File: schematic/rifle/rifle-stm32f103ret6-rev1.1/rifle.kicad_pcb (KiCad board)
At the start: 2 copper layers, 83.2 x 62.1 mm, 51 parts, among them K1 Magazine, K2 Sound, K3 IR_LASER, P1 Indication, P10 RFID-RC522-MODULE, P11 NRF24L01, P12 CONN_2, P13 IR_LED, P14 Power_in, P15 Power_out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

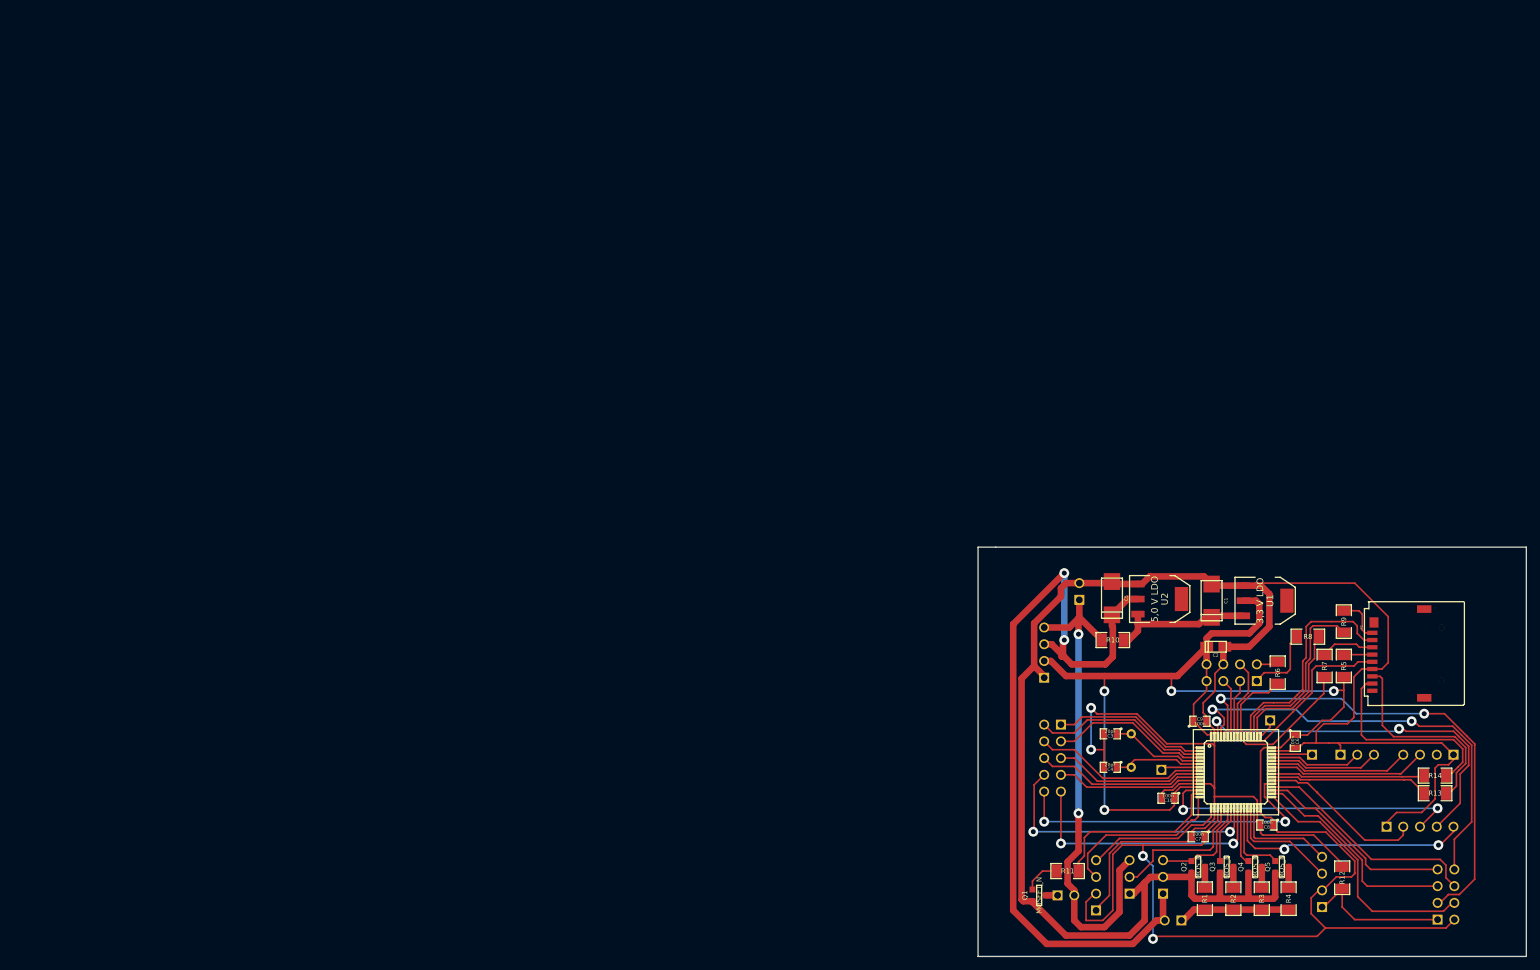
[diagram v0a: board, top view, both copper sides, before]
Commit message: Rifle r1.1 pcb beginned
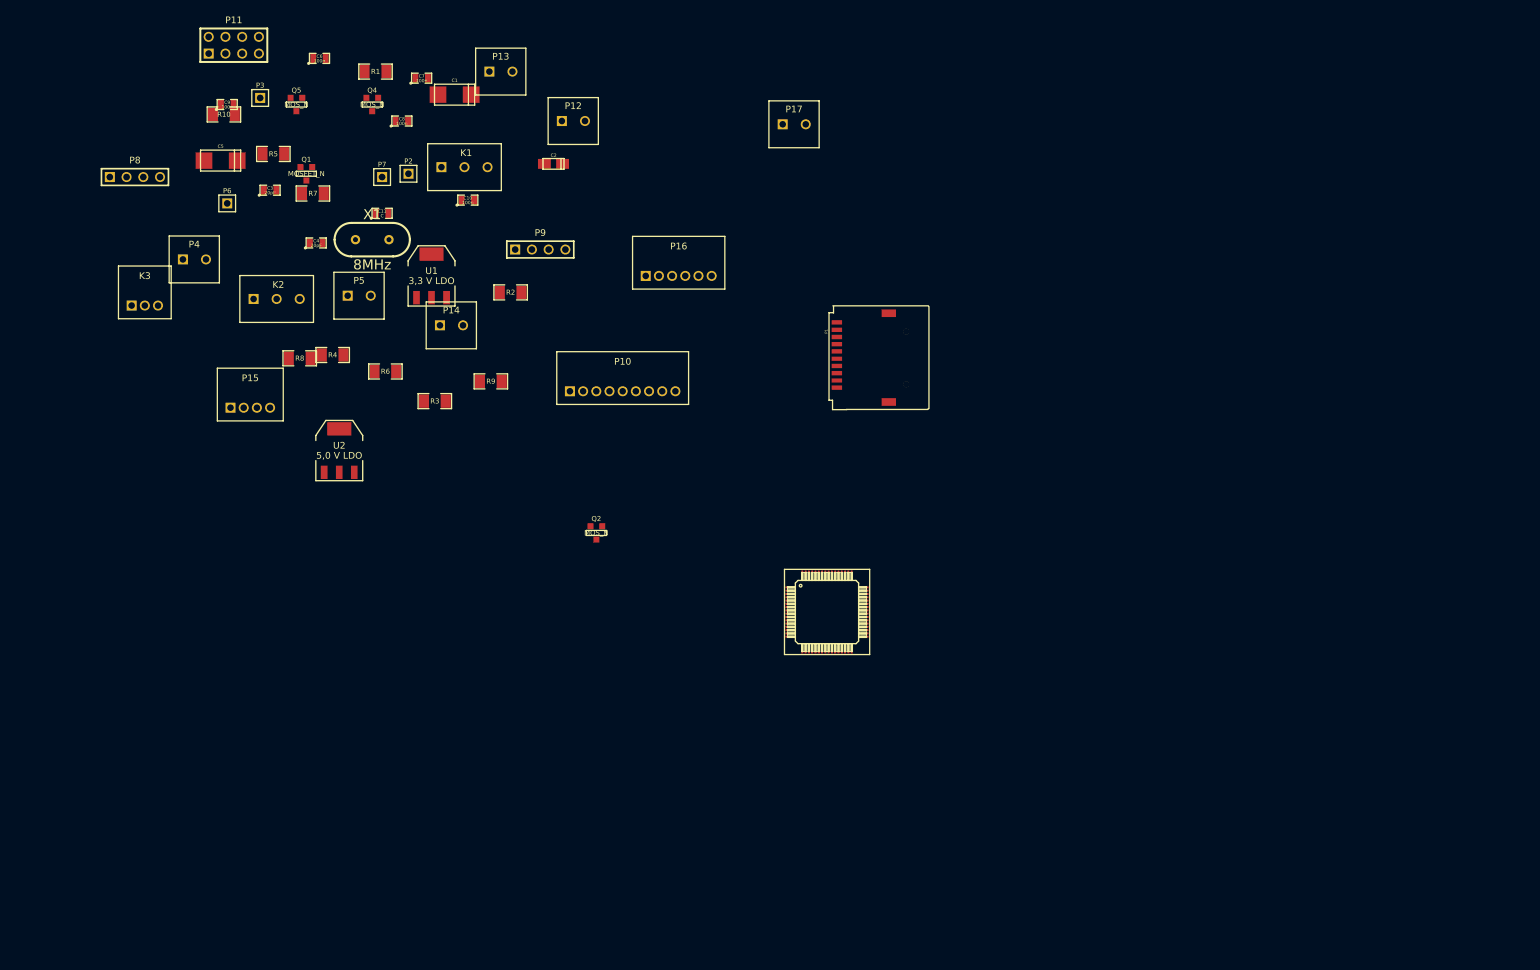
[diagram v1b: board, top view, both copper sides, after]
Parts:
- removed Q3: MOS_N, SOT23GDS
- removed R11, R12, R13, R14: 0, SM1206
- added C11: C, SM0805, F.Cu at (23.5, 22.5)
- added P16: Indicators, PIN_ARRAY-6X1-2mm-horiz, F.Cu at (68.5, 32.0)
- added P17: FireFlash, TERMINALS_2, F.Cu at (86.0, 9.00)
- K1: footprint PIN_ARRAY_3X1 -> TERMINALS_3; moved to F.Cu
- K2: value Sound -> Fire_mode; footprint PIN_ARRAY_3X1 -> TERMINALS_3; moved to F.Cu
- K3: footprint PIN_ARRAY_3X1 -> PIN_ARRAY-3X1-2mm-horiz; moved to F.Cu
- P1: value Indication -> MICROSD-SDIO-CD; footprint PIN_ARRAY_5x2 -> MICROSD-CD; moved to F.Cu
- P10: footprint pin_array_4x2 -> PIN_ARRAY-9X1-2mm-horiz; moved to F.Cu
- P11, P3, P6, P7, P8, P9, X1: moved to F.Cu
- P12: value CONN_2 -> VibroEng; footprint PIN_ARRAY_2X1 -> TERMINALS_2; moved to F.Cu
- P13, P14: footprint PIN_ARRAY_2X1 -> TERMINALS_2; moved to F.Cu
- P15: value Power_out -> Sound; footprint PIN_ARRAY_4x1 -> PIN_ARRAY-4X1-2mm-horiz; moved to F.Cu
- P2: value MICROSD-SDIO -> GND; footprint MICROSD -> PIN_ARRAY_1
- P4: value CONN_5 -> Reload; footprint PIN_ARRAY_5x1 -> TERMINALS_2; moved to F.Cu
- P5: value CONN_4 -> Fire; footprint PIN_ARRAY_4x1 -> TERMINALS_2; moved to F.Cu
- R1, R2: value R -> 47k
- R10, R8, R9: value 0 -> R
- R5, R6, R7: value 0 -> 47k
- moved P11 224.6 mm to (1.00, -3.00), turned to 0 degrees
- moved P4 204.9 mm to (-5.00, 29.5)
- moved Q5 189.0 mm to (10.5, 6.00), turned to 0 degrees
- moved P6 184.6 mm to (0.00, 21.0)
- moved P8 181.1 mm to (-14.0, 17.0), turned to 0 degrees
- moved C6 180.7 mm to (14.0, -1.00), turned to 0 degrees
- moved R5 180.0 mm to (7.00, 13.5), turned to 0 degrees
- moved R1 177.7 mm to (22.5, 1.00), turned to 0 degrees
- moved K3 177.1 mm to (-12.5, 36.5), turned to 0 degrees
- moved Q4 177.0 mm to (22.0, 6.00), turned to 0 degrees
- moved C9 174.7 mm to (0.00, 6.00)
- moved P5 171.1 mm to (20.0, 35.0), turned to 0 degrees
- moved P3 170.5 mm to (5.00, 5.00)
- moved R7 169.4 mm to (13.0, 19.5), turned to 0 degrees
- moved C8 169.2 mm to (26.5, 8.50), turned to 0 degrees
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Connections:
- C1 pad 1: N-0000049 -> +BATT
- K2 pad 2: N-0000063 -> N-0000032
- K2 pad 3: +BATT -> N-0000048
- K3 pad 3: N-0000058 -> N-000004
- P1 pad 1: N-0000057 -> N-0000035
- P1 pad 2: N-0000060 -> N-0000034
- P1 pad 3: N-0000061 -> N-0000033
- P1 pad 4: N-0000051 -> +3.3V
- P1 pad 5: N-0000052 -> N-0000016
- P1 pad 6: N-0000053 -> GND
- P1 pad 7: N-0000050 -> N-0000043
- P1 pad 8: N-0000069 -> N-0000053
- P10 pad 1: N-000009 (its old number) -> N-0000024
- P10 pad 2: N-0000033 -> N-0000051
- P11 pad 1: N-0000041 -> GND
- P13 pad 1: N-0000015 (its old number) -> N-0000030
- P15 pad 2: +3.3V -> N-0000040
- P15 pad 3: +5V -> N-0000044
- P2 pad 1: N-0000045 (its old number) -> GND
- P4 pad 2: N-0000035 -> N-0000050
- P5 pad 1: N-0000041 -> GND
- P5 pad 2: +3.3V -> N-0000031
- Q1 pad G: N-0000040 -> N-0000013
- Q2 pad D: N-0000016 -> N-0000038
- Q2 pad G: N-0000058 -> N-0000039
- Q4 pad G: N-0000013 -> N-000004
- R1 pad 1: N-0000015 (its old number) -> +3.3V
- R1 pad 2: N-0000016 -> N-0000053
- R10 pad 1: +BATT -> N-0000042
- R10 pad 2: N-0000049 -> N-0000040
- R2 pad 1: N-0000015 (its old number) -> +3.3V
- R2 pad 2: N-0000017 (its old number) -> N-0000043
- R3 pad 1: N-0000015 (its old number) -> N-0000030
- R4 pad 1: N-0000015 (its old number) -> N-0000030
- R5 pad 1: N-0000044 -> +3.3V
- R5 pad 2: +3.3V -> N-0000033
- R6 pad 1: N-0000034 -> +3.3V
- R6 pad 2: N-0000033 -> N-0000034
- R7 pad 1: N-0000047 (its old number) -> +3.3V
- R7 pad 2: N-0000056 -> N-0000035
- R8 pad 1: N-0000048 -> +BATT
- R8 pad 2: N-000009 (its old number) -> N-0000052
- R9 pad 1: N-0000045 (its old number) -> N-0000052
- R9 pad 2: N-0000046 -> GND
- U1 pad 3: N-0000049 -> +BATT
- U2 pad 3: N-0000049 -> +BATT
- U3 pad 10: N-0000053 -> (no net)
- U3 pad 11: N-0000050 -> (no net)
- U3 pad 14: N-0000038 -> N-0000031
- U3 pad 15: N-0000064 -> N-0000013
- U3 pad 2: N-0000057 -> (no net)
- U3 pad 20: N-0000063 -> N-0000042
- U3 pad 21: (no net) -> N-0000049
- U3 pad 22: N-0000058 -> N-0000046
- U3 pad 24: N-0000069 -> N-0000044
- U3 pad 25: N-0000070 -> (no net)
- U3 pad 26: N-0000013 -> N-000004
- U3 pad 28: N-0000032 -> N-0000050
- U3 pad 29: N-0000010 (its old number) -> (no net)
- U3 pad 3: N-0000060 -> (no net)
- U3 pad 30: N-0000011 (its old number) -> N-0000039
- U3 pad 37: N-0000062 -> N-0000032
- U3 pad 38: N-0000035 -> N-0000036
- U3 pad 39: N-0000068 -> N-0000043
- U3 pad 4: N-0000061 -> (no net)
- U3 pad 40: N-0000059 -> N-0000053
- U3 pad 41: (no net) -> N-0000054
- U3 pad 50: N-0000048 -> N-0000024
- U3 pad 51: N-0000046 -> N-0000035
- U3 pad 52: N-0000054 -> N-0000034
- U3 pad 53: N-0000055 -> N-0000016
- U3 pad 54: N-0000056 -> N-0000033
- U3 pad 55: N-0000034 -> N-0000051
- U3 pad 62: N-0000039 -> N-0000048
- U3 pad 8: N-0000051 -> N-0000052
- U3 pad 9: N-0000052 -> (no net)
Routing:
- net GND: track 391.3 -> 0.00 mm, vias 2 -> 0
- net +3.3V: track 288.3 -> 0.00 mm, vias 6 -> 0
- net +5V: track 121.9 -> 0.00 mm, vias 2 -> 0
- net +BATT: track 77.2 -> 0.00 mm, vias 2 -> 0
- net N-000001: track 74.9 -> 0.00 mm, vias 2 -> 0
- net N-0000011: track 66.6 -> 0.00 mm, vias 2 -> 0
- net N-0000039: track 56.5 -> 0.00 mm, vias 2 -> 0
- net N-0000062: track 49.5 -> 0.00 mm, vias 2 -> 0
- net N-0000038: track 48.3 -> 0.00 mm, vias 2 -> 0
- net N-0000069: track 42.7 -> 0.00 mm, vias 2 -> 0
- net N-0000070: track 39.4 -> 0.00 mm, vias 2 -> 0
- net N-0000010: track 38.4 -> 0.00 mm
- net N-0000032: track 38.4 -> 0.00 mm, vias 2 -> 0
- net N-000008: track 34.8 -> 0.00 mm
- net N-0000054: track 34.4 -> 0.00 mm
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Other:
- board outline removed
- net class Batt+ removed
- net class Default: clearance 0.2 -> 0.254; trace_width 1 -> 0.254; via_dia 1.5 -> 0.889; via_drill 1 -> 0.635
- rule trace_clearance: 0.2 -> 0.254

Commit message: WIP rifle 1.1 pcb
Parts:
- K1, K2, K3, P10, P11, P12, P13, P14, P15, P16, P17, P2, P3, P4, P5, P6, P7, P8, P9, X1: moved to B.Cu
- moved P11 140.3 mm to (108.8, 86.8), turned to 90 degrees
- moved P4 124.0 mm to (99.2, 96.7)
- moved K3 118.5 mm to (91.0, 94.3)
- moved P6 115.6 mm to (99.8, 79.4)
- moved P15 114.6 mm to (104.8, 105.5)
- moved P14 110.1 mm to (135.6, 81.8)
- moved P8 110.0 mm to (64.5, 94.1), turned to 270 degrees
- moved P3 107.4 mm to (77.8, 83.9)
- moved C8 107.2 mm to (97.0, 89.2)
- moved C6 104.4 mm to (85.0, 75.5), turned to 90 degrees
- moved C7 97.8 mm to (82.2, 84.4), turned to 90 degrees
- moved K1 94.3 mm to (107.1, 77.4)
- moved P7 93.2 mm to (96.5, 75.0)
- moved C3 92.5 mm to (79.0, 76.5), turned to 180 degrees
- moved P17 90.4 mm to (107.9, 96.7)
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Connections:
- P17 pad 2: (no net) -> +3.3V
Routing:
- net +3.3V: track 0.00 -> 15.5 mm
- net N-0000013: track 0.00 -> 11.8 mm
- net GND: track 0.00 -> 9.65 mm, vias 0 -> 5
- net N-0000023: track 0.00 -> 3.45 mm
- added copper zone on F.Cu, net +3.3V
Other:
- net class Default: clearance 0.254 -> 0.18; trace_width 0.254 -> 0.3; via_dia 0.889 -> 0.7; via_drill 0.635 -> 0.3
- rule trace_clearance: 0.254 -> 0.18
- rule trace_min: 0.254 -> 0.15
- rule via_min_drill: 0.508 -> 0.3
- rule via_min_size: 0.889 -> 0.7

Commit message: Rifle pcb seems done
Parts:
- P8: footprint PIN_ARRAY_4x1 -> PIN_ARRAY-4X1-2mm-horiz
- moved Q5 124.1 mm to (93.9, 97.9)
- moved C9 115.9 mm to (97.5, 68.6), turned to 270 degrees
- moved Q4 111.1 mm to (84.4, 97.9)
- moved R10 103.1 mm to (66.5, 85.8), turned to 90 degrees
- moved C5 102.5 mm to (84.3, 71.4), turned to 180 degrees
- moved R5 101.9 mm to (95.8, 63.5), turned to 90 degrees
- moved Q1 100.3 mm to (82.3, 88.0)
- moved R1 97.5 mm to (92.3, 69.0), turned to 270 degrees
- moved R4 91.0 mm to (89.2, 98.1)
- moved R7 89.1 mm to (90.5, 63.5), turned to 90 degrees
- moved R6 71.2 mm to (93.1, 63.5), turned to 90 degrees
- moved P14 67.8 mm to (72.8, 56.2)
- moved R3 67.0 mm to (79.6, 97.7)
- moved U1 62.6 mm to (84.2, 64.9), turned to 180 degrees
- moved P2 61.4 mm to (99.1, 55.9)
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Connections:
- P17 pad 2: +3.3V -> +BATT
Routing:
- net +BATT: track 0.00 -> 143.2 mm, vias 0 -> 2
- net +3.3V: track 15.5 -> 109.3 mm, vias 0 -> 6
- net GND: track 9.65 -> 73.6 mm, vias 5 -> 21
- net N-0000037: track 0.00 -> 60.7 mm
- net +5V: track 0.00 -> 58.4 mm, vias 0 -> 1
- net N-0000010: track 0.00 -> 40.5 mm, vias 0 -> 2
- net N-0000034: track 0.00 -> 37.5 mm
- net N-0000033: track 0.00 -> 37.1 mm, vias 0 -> 2
- net N-0000035: track 0.00 -> 37.1 mm, vias 0 -> 2
- net N-0000054: track 0.00 -> 36.8 mm
- net N-000009: track 0.00 -> 32.8 mm, vias 0 -> 2
- net N-0000042: track 0.00 -> 28.8 mm, vias 0 -> 2
- net N-0000032: track 0.00 -> 28.3 mm, vias 0 -> 2
- net N-0000053: track 0.00 -> 27.8 mm, vias 0 -> 1
- net N-0000047: track 0.00 -> 26.3 mm, vias 0 -> 4
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- added copper zone on B.Cu, net GND
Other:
- board outline added: 50.3 x 48 mm
- net class Default: trace_width 0.3 -> 0.6

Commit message: Rifle design seems done
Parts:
- added 1PIN: P***, 1pin, F.Cu at (109.5, 56.0)
- added 1PIN: P***, 1pin, F.Cu at (104.0, 56.0)
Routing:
- net GND: track 73.6 -> 82.2 mm, vias 21 -> 22
- net +3.3V: track 109.3 -> 114.6 mm
- net N-000009: track 32.8 -> 29.0 mm, vias 2 -> 4
- net N-0000010: track 40.5 -> 37.1 mm, vias 2 -> 4
- net +BATT: track 143.2 -> 142.2 mm
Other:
- board size 50.3 x 48 mm -> 49.2 x 48.2 mm
